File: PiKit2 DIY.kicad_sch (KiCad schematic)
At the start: 36 parts, among them J1 Conn_01x06_Socket, J2 USB_A, Q1 2N3904, Q2 2N3904, Q3 2N3906, Q4 2N3904, SW1 SW_Push, U1 PIC18F2550-ISP, X1 20Mhz

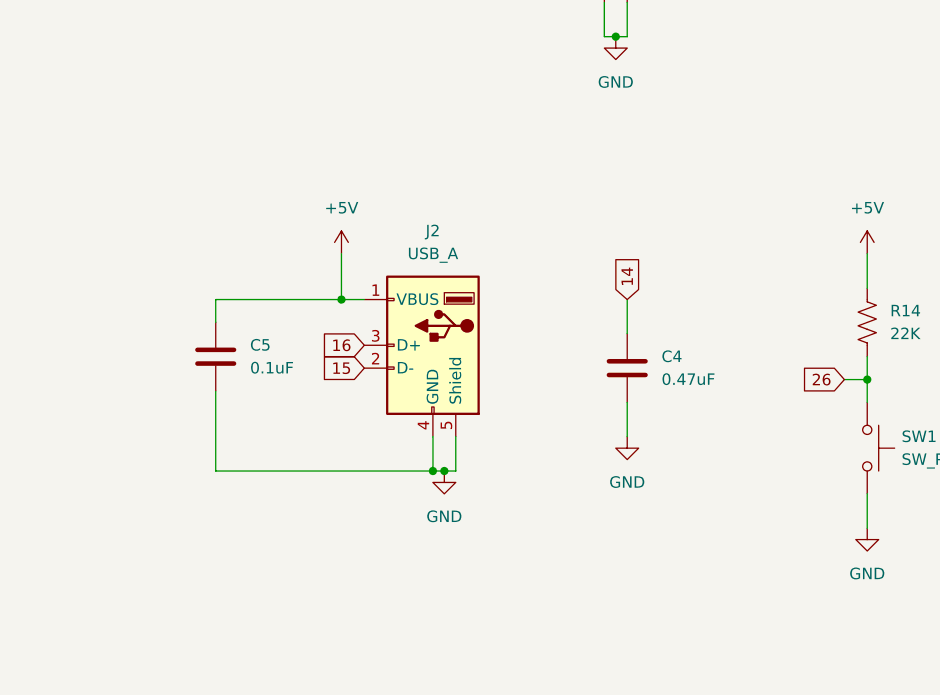
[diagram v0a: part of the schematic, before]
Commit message: Imported JLCPCB Footprints and 3D Models
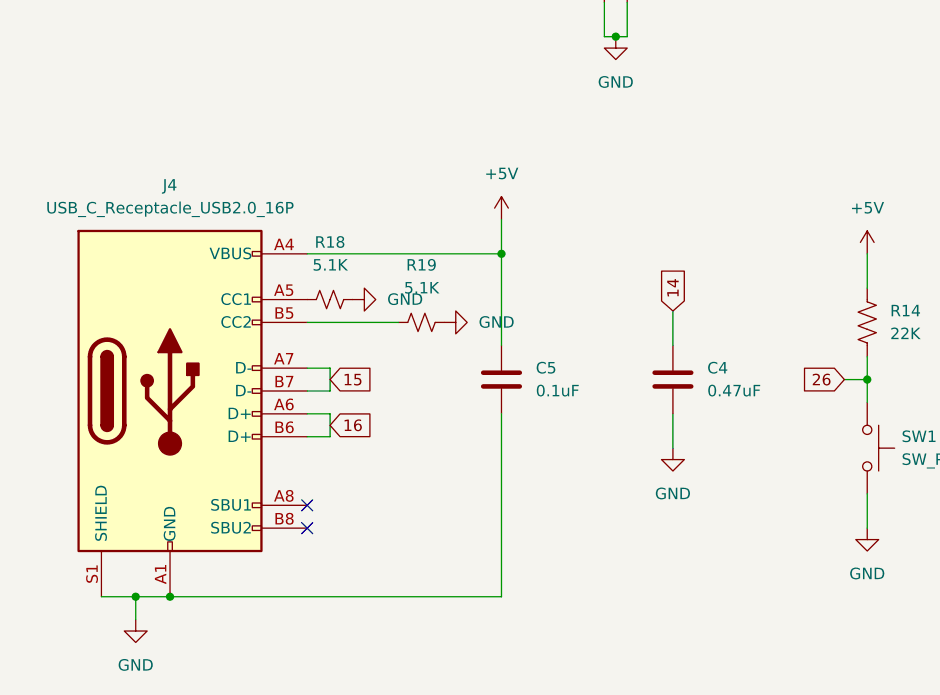
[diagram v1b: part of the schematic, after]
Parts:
- removed J2: USB_A, symbol Connector:USB_A
- added J4: USB_C_Receptacle_USB2.0_16P, JLCImport:KH-TYPE-C-16P, symbol Connector:USB_C_Receptacle_USB2.0_16P
- added R18, R19: 5.1K, symbol Device:R_Small_US
- C4: footprint (none) -> JLCImport:178MU0009
- C5: footprint (none) -> JLCImport:178MU0006
- D1: footprint Diode_THT:D_DO-35_SOD27_P7.62mm_Horizontal -> JLCImport:BAT41
- D2: footprint Diode_THT:D_DO-41_SOD81_P10.16mm_Horizontal -> JLCImport:1N5817_C7544876
- D3, D4: footprint (none) -> LED_THT:LED_D5.0mm
- J1: footprint (none) -> JLCImport:2_54-1_6PHeader-RA
- L1: footprint (none) -> JLCImport:YAL0410-681K
- Q1, Q2, Q4: footprint Package_TO_SOT_THT:TO-92_Inline -> JLCImport:2N3904_C2874602
- Q3: footprint Package_TO_SOT_THT:TO-92_Inline -> JLCImport:2N3906_C2874603
- SW1: footprint (none) -> Button_Switch_THT:SW_PUSH_6mm
- X1: footprint (none) -> JLCImport:X49ST2-20_000-F20JGDT
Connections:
- net +5V: now also J4.A4 (VBUS), J4.A9 (VBUS), J4.B4 (VBUS), J4.B9 (VBUS)
- net 15: now also J4.A7 (D-), J4.B7 (D-)
- net 16: now also J4.A6 (D+), J4.B6 (D+)
- net GND: now also J4.A1 (GND), J4.A12 (GND), J4.B1 (GND), J4.B12 (GND), J4.S1 (SHIELD), R18.2, R19.2
- new net: J4.A5 (CC1), R18.1
- new net: J4.B5 (CC2), R19.1
- no-connect marks 10 -> 12
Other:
- moved on the sheet: C4, C5

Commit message: Added Resistor Footprints and models
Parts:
- R1: footprint (none) -> JLCImport:MF1_4W-1K_1_T52
- R10, R15, R16, R2: footprint (none) -> JLCImport:MF1_4W-4_7K_1_T52
- R11, R7: footprint (none) -> JLCImport:MFR0W4F3300A50
- R12, R13, R17, R8: footprint (none) -> JLCImport:MFR02SF1000A10
- R14: footprint (none) -> JLCImport:MF1_4W-22K_1_T52
- R18, R19: footprint (none) -> JLCImport:MF1_4W-5_1K_1_T52
- R3: footprint (none) -> JLCImport:MF1_4W-2_7K_1_T52
- R4: footprint (none) -> JLCImport:MF1_4W-100K_1_T52
- R5, R6, R9: footprint (none) -> JLCImport:MFR0W4F1002A50
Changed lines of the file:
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@@
 			)
 		)
-		(property "Footprint" ""
+		(property "Footprint" "JLCImport:MF1_4W-4_7K_1_T52"
 			(at 216.154 59.944 90)
 			(effects
@@
 			)
 		)
-		(property "Footprint" ""
+		(property "Footprint" "JLCImport:MF1_4W-4_7K_1_T52"
 			(at 221.234 59.436 90)
 			(effects
@@
 			)
 		)
-		(property "Footprint" ""
+		(property "Footprint" "JLCImport:MFR02SF1000A10"
 			(at 193.294 49.784 90)
 			(effects
@@
 			)
 		)
-		(property "Footprint" ""
+		(property "Footprint" "JLCImport:MF1_4W-100K_1_T52"
 			(at 209.296 75.184 90)
 			(effects
@@
 			)
 		)
-		(property "Footprint" ""
+		(property "Footprint" "JLCImport:MF1_4W-5_1K_1_T52"
 			(at 48.26 125.73 0)
 			(effects
@@
 			)
 		)
-		(property "Footprint" ""
+		(property "Footprint" "JLCImport:MFR0W4F1002A50"
 			(at 194.564 98.044 90)
 			(effects
@@
 			)
 		)
-		(property "Footprint" ""
+		(property "Footprint" "JLCImport:MF1_4W-4_7K_1_T52"
 			(at 200.914 67.564 90)
 			(effects
@@
 			)
 		)
-		(property "Footprint" ""
+		(property "Footprint" "JLCImport:MFR0W4F1002A50"
 			(at 209.296 86.614 90)
 			(effects
@@
 			)
 		)
-		(property "Footprint" ""
+		(property "Footprint" "JLCImport:MF1_4W-5_1K_1_T52"
 			(at 58.42 128.27 0)
 			(effects
@@
 			)
 		)
-		(property "Footprint" ""
+		(property "Footprint" "JLCImport:MFR02SF1000A10"
 			(at 204.724 47.244 90)
 			(effects
@@
 			)
 		)
-		(property "Footprint" ""
+		(property "Footprint" "JLCImport:MFR02SF1000A10"
 			(at 212.344 52.324 90)
 			(effects
@@
 			)
 		)
-		(property "Footprint" ""
+		(property "Footprint" "JLCImport:MF1_4W-4_7K_1_T52"
 			(at 214.884 42.164 90)
 			(effects
@@
 			)
 		)
-		(property "Footprint" ""
+		(property "Footprint" "JLCImport:MF1_4W-22K_1_T52"
 			(at 108.966 128.524 90)
 			(effects
@@
 			)
 		)
-		(property "Footprint" ""
+		(property "Footprint" "JLCImport:MF1_4W-1K_1_T52"
 			(at 150.114 82.804 90)
 			(effects
@@
 			)
 		)
-		(property "Footprint" ""
+		(property "Footprint" "JLCImport:MFR0W4F1002A50"
 			(at 214.376 117.094 90)
 			(effects
@@
 			)
 		)
-		(property "Footprint" ""
+		(property "Footprint" "JLCImport:MFR0W4F3300A50"
 			(at 178.816 137.414 90)
 			(effects
@@
 			)
 		)
-		(property "Footprint" ""
+		(property "Footprint" "JLCImport:MF1_4W-2_7K_1_T52"
 			(at 190.246 76.454 90)
 			(effects
@@
 			)
 		)
-		(property "Footprint" ""
+		(property "Footprint" "JLCImport:MFR0W4F3300A50"
 			(at 162.306 137.414 90)
 			(effects
@@
 			)
 		)
-		(property "Footprint" ""
+		(property "Footprint" "JLCImport:MFR02SF1000A10"
 			(at 223.266 94.234 90)
 			(effects

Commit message: Import full PCB, fix schematic label, add backups
Replace PiKit2 DIY.kicad_pcb with the full KiCad 9 PCB data (generated by pcbnew). Update PiKit2 DIY.kicad_sch global_label from "9" to "7". Add four backup zip archives under PiKit2 DIY-backups for recent snapshots.
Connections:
- net 7: now also R9.2
- net 9: no longer R9.2
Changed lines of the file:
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@@
 		)
 	)
-	(global_label "9"
+	(global_label "7"
 		(shape input)
 		(at 213.36 120.65 270)

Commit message: Updated 100 ohm R model and footprint; Finished component placement; began routing traces
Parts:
- R12, R13, R17, R8: footprint JLCImport:MFR02SF1000A10 -> JLCImport:MFR0W4F1000A50
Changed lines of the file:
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@@
 			)
 		)
-		(property "Footprint" "JLCImport:MFR02SF1000A10"
+		(property "Footprint" "JLCImport:MFR0W4F1000A50"
 			(at 193.294 49.784 90)
 			(effects
@@
 			)
 		)
-		(property "Footprint" "JLCImport:MFR02SF1000A10"
+		(property "Footprint" "JLCImport:MFR0W4F1000A50"
 			(at 204.724 47.244 90)
 			(effects
@@
 			)
 		)
-		(property "Footprint" "JLCImport:MFR02SF1000A10"
+		(property "Footprint" "JLCImport:MFR0W4F1000A50"
 			(at 212.344 52.324 90)
 			(effects
@@
 			)
 		)
-		(property "Footprint" "JLCImport:MFR02SF1000A10"
+		(property "Footprint" "JLCImport:MFR0W4F1000A50"
 			(at 223.266 94.234 90)
 			(effects

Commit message: KiCad: add stackup, fix nets and footprints
Add PCB stackup and layer definitions; remap many net indices and correct USB D+/D- nets and Type-C pin mappings. Adjust footprint positions, pad orientations and UUIDs, update routing (including a tuned pattern for a route), and fix silkscreen geometry. Update schematic: add D+/D- labels/wires and remove redundant global labels. Add/remove several backup zip files. These edits correct net assignments, improve component placement/orientation and refine USB routing.
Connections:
- net 15 renamed D-
- net 16 renamed D+
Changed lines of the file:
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@@
+	(wire
+		(pts
+			(xy 116.84 46.99) (xy 111.76 46.99)
+		)
+		(stroke
+			(width 0)
+			(type default)
+		)
+	)
 	(wire
 		(pts
@@
 	(wire
 		(pts
+			(xy 116.84 49.53) (xy 111.76 49.53)
+		)
+		(stroke
+			(width 0)
+			(type default)
+		)
+	)
+	(wire
+		(pts
 			(xy 156.21 76.2) (xy 152.4 76.2)
 		)
@@
 		)
 	)
+	(label "D+"
+		(at 48.26 139.7 0)
+		(effects
+			(font
+				(size 1.27 1.27)
+			)
+			(justify left bottom)
+		)
+	)
+	(label "D-"
+		(at 48.26 134.62 0)
+		(effects
+			(font
+				(size 1.27 1.27)
+			)
+			(justify left bottom)
+		)
+	)
+	(label "D+"
+		(at 113.03 49.53 0)
+		(effects
+			(font
+				(size 1.27 1.27)
+			)
+			(justify left bottom)
+		)
+	)
+	(label "D-"
+		(at 115.57 46.99 0)
+		(effects
+			(font
+				(size 1.27 1.27)
+			)
+			(justify left bottom)
+		)
+	)
 	(global_label "11"
 		(shape input)
@@
 		)
 	)
-	(global_label "16"
-		(shape input)
-		(at 111.76 49.53 0)
+	(global_label "6"
+		(shape input)
+		(at 208.28 53.34 180)
+		(fields_autoplaced yes)
+		(effects
+			(font
+				(size 1.27 1.27)
+			)
+			(justify right)
+		)
+		(property "Intersheetrefs" "${INTERSHEET_REFS}"
+			(at 204.0853 53.34 0)
+			(effects
+				(font
+					(size 1.27 1.27)
+				)
+				(justify right)
+				(hide yes)
+			)
+		)
+	)
+	(global_label "26"
+		(shape input)
+		(at 50.8 77.47 180)
+		(fields_autoplaced yes)
+		(effects
+			(font
+				(size 1.27 1.27)
+			)
+			(justify right)
+		)
+		(property "Intersheetrefs" "${INTERSHEET_REFS}"
+			(at 45.3958 77.47 0)
+			(effects
+				(font
+					(size 1.27 1.27)
+				)
+				(justify right)
+				(hide yes)
+			)
+		)
+	)
+	(global_label "5"
+		(shape input)
+		(at 189.23 50.8 180)
+		(fields_autoplaced yes)
+		(effects
+			(font
+				(size 1.27 1.27)
+			)
+			(justify right)
+		)
+		(property "Intersheetrefs" "${INTERSHEET_REFS}"
+			(at 185.0353 50.8 0)
+			(effects
+				(font
+					(size 1.27 1.27)
+				)
+				(justify right)
+				(hide yes)
+			)
+		)
+	)
+	(global_label "3"
+		(shape input)
+		(at 50.8 41.91 180)
+		(fields_autoplaced yes)
+		(effects
+			(font
+				(size 1.27 1.27)
+			)
+			(justify right)
+		)
+		(property "Intersheetrefs" "${INTERSHEET_REFS}"
+			(at 46.6053 41.91 0)
+			(effects
+				(font
+					(size 1.27 1.27)
+				)
+				(justify right)
+				(hide yes)
+			)
+		)
+	)
+	(global_label "7"
+		(shape input)
+		(at 50.8 52.07 180)
+		(fields_autoplaced yes)
+		(effects
+			(font
+				(size 1.27 1.27)
+			)
+			(justify right)
+		)
+		(property "Intersheetrefs" "${INTERSHEET_REFS}"
+			(at 46.6053 52.07 0)
+			(effects
+				(font
+					(size 1.27 1.27)
+				)
+				(justify right)
+				(hide yes)
+			)
+		)
+	)
+	(global_label "23"
+		(shape input)
+		(at 50.8 69.85 180)
+		(fields_autoplaced yes)
+		(effects
+			(font
+				(size 1.27 1.27)
+			)
+			(justify right)
+		)
+		(property "Intersheetrefs" "${INTERSHEET_REFS}"
+			(at 45.3958 69.85 0)
+			(effects
+				(font
+					(size 1.27 1.27)
+				)
+				(justify right)
+				(hide yes)
+			)
+		)
+	)
+	(global_label "14"
+		(shape input)
+		(at 86.36 127 90)
 		(fields_autoplaced yes)
 		(effects
@@
 		)
 		(property "Intersheetrefs" "${INTERSHEET_REFS}"
-			(at 117.1642 49.53 0)
-			(effects
-				(font
-					(size 1.27 1.27)
-				)
-				(justify left)
-				(hide yes)
-			)
-		)
-	)
-	(global_label "6"
-		(shape input)
-		(at 208.28 53.34 180)
+			(at 86.36 121.5958 90)
+			(effects
+				(font
+					(size 1.27 1.27)
+				)
+				(justify left)
+				(hide yes)
+			)
+		)
+	)
+	(global_label "12"
+		(shape input)
+		(at 140.97 83.82 180)
 		(fields_autoplaced yes)
 		(effects
@@
 		)
 		(property "Intersheetrefs" "${INTERSHEET_REFS}"
-			(at 204.0853 53.34 0)
-			(effects
-				(font
-					(size 1.27 1.27)
-				)
-				(justify right)
-				(hide yes)
-			)
-		)
-	)
-	(global_label "26"
-		(shape input)
-		(at 50.8 77.47 180)
-		(fields_autoplaced yes)
-		(effects
-			(font
-				(size 1.27 1.27)
-			)
-			(justify right)
-		)
-		(property "Intersheetrefs" "${INTERSHEET_REFS}"
-			(at 45.3958 77.47 0)
-			(effects
-				(font
-					(size 1.27 1.27)
-				)
-				(justify right)
-				(hide yes)
-			)
-		)
-	)
-	(global_label "15"
-		(shape input)
-		(at 111.76 46.99 0)
-		(fields_autoplaced yes)
-		(effects
-			(font
-				(size 1.27 1.27)
-			)
-			(justify left)
-		)
-		(property "Intersheetrefs" "${INTERSHEET_REFS}"
-			(at 117.1642 46.99 0)
-			(effects
-				(font
-					(size 1.27 1.27)
-				)
-				(justify left)
-				(hide yes)
-			)
-		)
-	)
-	(global_label "5"
-		(shape input)
-		(at 189.23 50.8 180)
-		(fields_autoplaced yes)
-		(effects
-			(font
-				(size 1.27 1.27)
-			)
-			(justify right)
-		)
-		(property "Intersheetrefs" "${INTERSHEET_REFS}"
-			(at 185.0353 50.8 0)
-			(effects
-				(font
-					(size 1.27 1.27)
-				)
-				(justify right)
-				(hide yes)
-			)
-		)
-	)
-	(global_label "3"
-		(shape input)
-		(at 50.8 41.91 180)
-		(fields_autoplaced yes)
-		(effects
-			(font
-				(size 1.27 1.27)
-			)
-			(justify right)
-		)
-		(property "Intersheetrefs" "${INTERSHEET_REFS}"
-			(at 46.6053 41.91 0)
-			(effects
-				(font
-					(size 1.27 1.27)
-				)
-				(justify right)
-				(hide yes)
-			)
-		)
-	)
-	(global_label "15"
-		(shape input)
-		(at 48.26 134.62 0)
-		(fields_autoplaced yes)
-		(effects
-			(font
-				(size 1.27 1.27)
-			)
-			(justify left)
-		)
-		(property "Intersheetrefs" "${INTERSHEET_REFS}"
-			(at 53.6642 134.62 0)
-			(effects
-				(font
-					(size 1.27 1.27)
-				)
-				(justify left)
-				(hide yes)
-			)
-		)
-	)
-	(global_label "7"
-		(shape input)
-		(at 50.8 52.07 180)
-		(fields_autoplaced yes)
-		(effects
-			(font
-				(size 1.27 1.27)
-			)
-			(justify right)
-		)
-		(property "Intersheetrefs" "${INTERSHEET_REFS}"
-			(at 46.6053 52.07 0)
-			(effects
-				(font
-					(size 1.27 1.27)
-				)
-				(justify right)
-				(hide yes)
-			)
-		)
-	)
-	(global_label "23"
-		(shape input)
-		(at 50.8 69.85 180)
-		(fields_autoplaced yes)
-		(effects
-			(font
-				(size 1.27 1.27)
-			)
-			(justify right)
-		)
-		(property "Intersheetrefs" "${INTERSHEET_REFS}"
-			(at 45.3958 69.85 0)
-			(effects
-				(font
-					(size 1.27 1.27)
-				)
-				(justify right)
-				(hide yes)
-			)
-		)
-	)
-	(global_label "14"
-		(shape input)
-		(at 86.36 127 90)
-		(fields_autoplaced yes)
-		(effects
-			(font
-				(size 1.27 1.27)
-			)
-			(justify left)
-		)
-		(property "Intersheetrefs" "${INTERSHEET_REFS}"
-			(at 86.36 121.5958 90)
-			(effects
-				(font
-					(size 1.27 1.27)
-				)
-				(justify left)
-				(hide yes)
-			)
-		)
-	)
-	(global_label "12"
-		(shape input)
-		(at 140.97 83.82 180)
-		(fields_autoplaced yes)
-		(effects
-			(font
-				(size 1.27 1.27)
-			)
-			(justify right)
-		)
-		(property "Intersheetrefs" "${INTERSHEET_REFS}"
 			(at 135.5658 83.82 0)
 			(effects
@@
 				)
 				(justify right)
-				(hide yes)
-			)
-		)
-	)
-	(global_label "16"
-		(shape input)
-		(at 48.26 139.7 0)
-		(fields_autoplaced yes)
-		(effects
-			(font
-				(size 1.27 1.27)
-			)
-			(justify left)
-		)
-		(property "Intersheetrefs" "${INTERSHEET_REFS}"
-			(at 53.6642 139.7 0)
-			(effects
-				(font
-					(size 1.27 1.27)
-				)
-				(justify left)
 				(hide yes)
 			)
@@
 		(on_board yes)
 		(dnp no)
-		(fields_autoplaced yes)
 		(property "Reference" "R2"
 			(at 200.66 62.23 90)

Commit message: Update to images
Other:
- title: (none) -> PicKit 2 DIY Clone
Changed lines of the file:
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@@
 	(generator_version "9.0")
 	(paper "A4")
+	(title_block
+		(title "PicKit 2 DIY Clone")
+		(date "2026-08-13")
+		(rev "1.0")
+	)
 	(junction
 		(at 67.31 120.65)
